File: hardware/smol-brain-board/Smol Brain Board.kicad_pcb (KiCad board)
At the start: 2 copper layers, 67 parts, among them J1 USB4085-GF-A, J10 Jumper 2Way Vert Solderable, J12 Jumper 2Way Vert Solderable, J3 CAN_DBG, J4 Jumper 2Way Vert Solderable, J5 Jumper 2Way Vert Solderable, J6 Smol_Brain_Board, J7 PROGRAM, J8 Jumper 2Way Vert Solderable, J9 Jumper 2Way Vert Solderable, U1 ESP32-S3-WROOM-1-N8, U3 SN65HVD231D

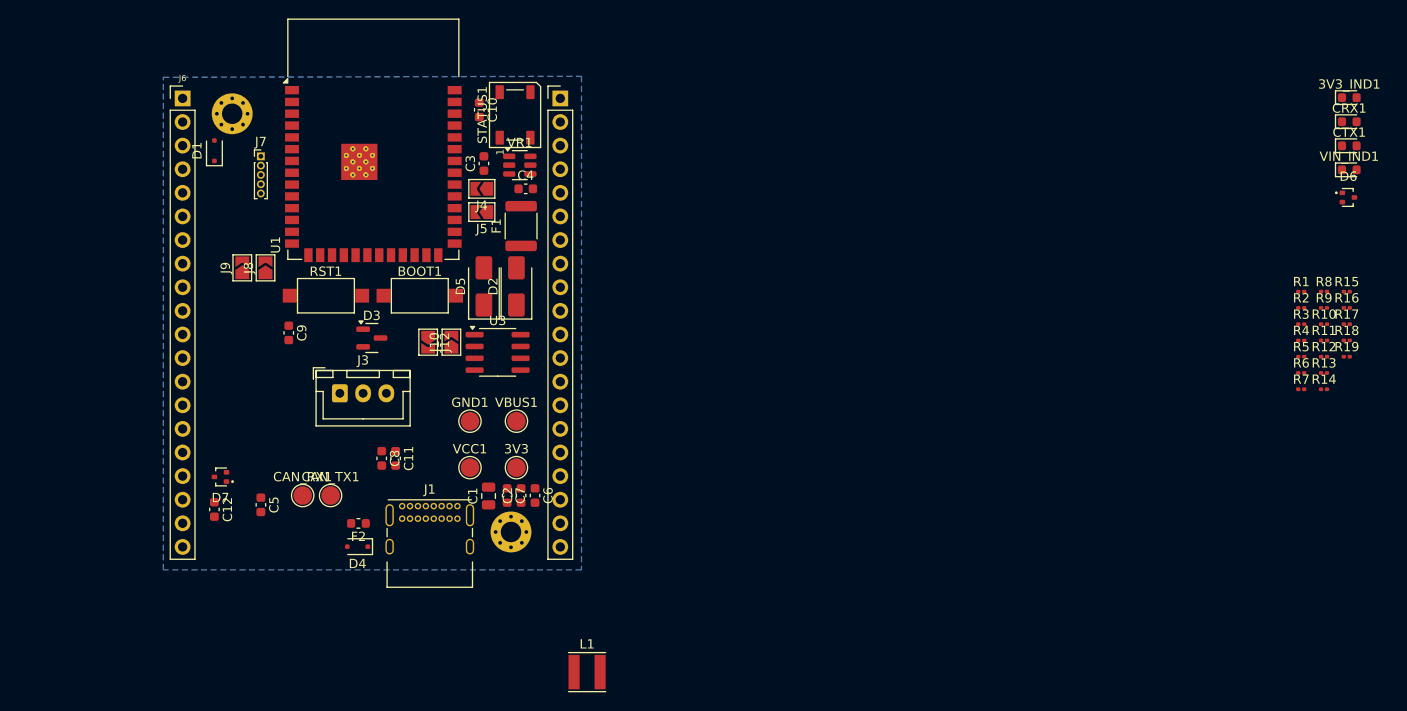
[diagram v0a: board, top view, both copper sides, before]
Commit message: Silkscreen labels and moving stuff around
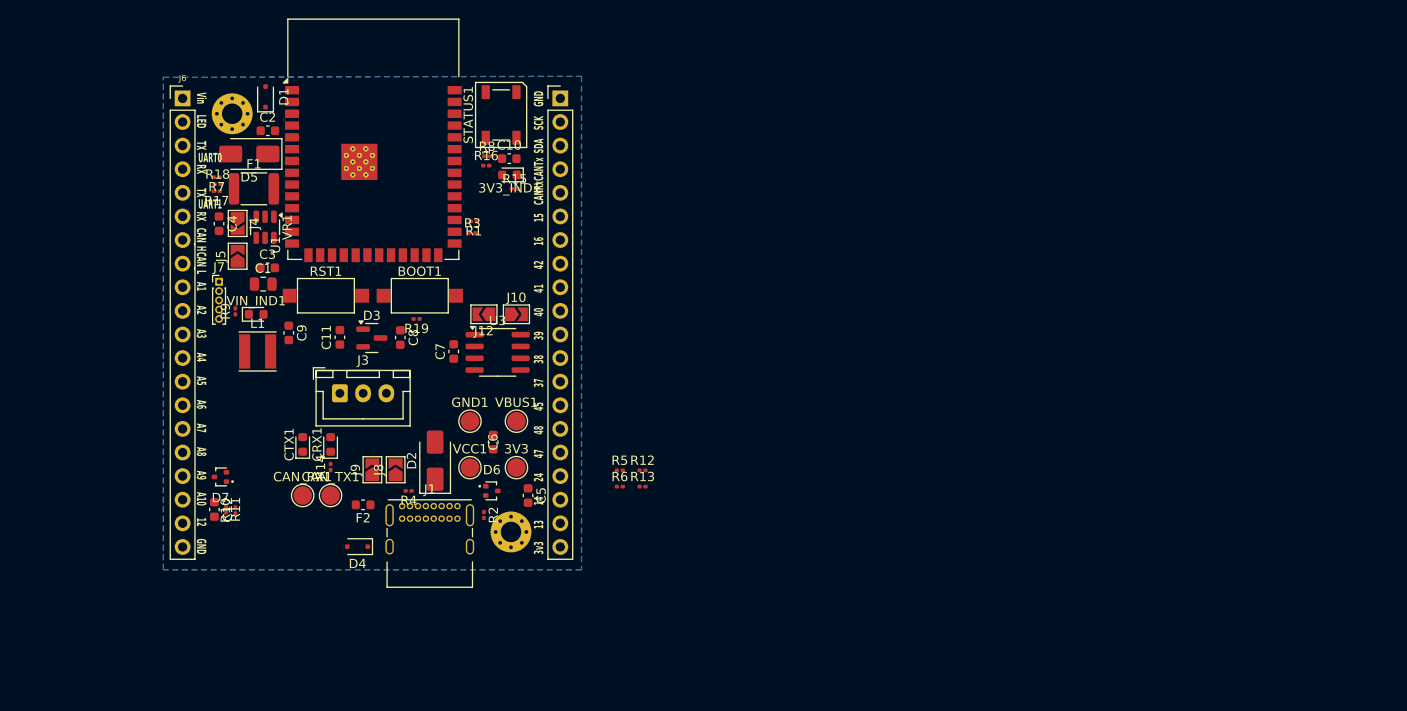
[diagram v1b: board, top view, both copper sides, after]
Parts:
- moved R18 122.7 mm to (131.9, 90.2)
- moved R17 122.4 mm to (131.9, 91.0), turned to 180 degrees
- moved R11 119.5 mm to (132.9, 125.2), turned to -90 degrees
- moved R7 118.9 mm to (131.9, 89.5), turned to 180 degrees
- moved R10 118.8 mm to (133.9, 125.3), turned to 90 degrees
- moved VIN_IND1 118.6 mm to (136.1, 104.2)
- moved R9 117.1 mm to (133.9, 103.9), turned to 90 degrees
- moved CTX1 117.1 mm to (141.1, 118.2), turned to 90 degrees
- moved CRX1 115.0 mm to (144.1, 118.2), turned to 90 degrees
- moved R14 107.2 mm to (144.1, 120.7), turned to 90 degrees
- moved R19 100.2 mm to (153.4, 104.7), turned to 180 degrees
- moved D6 97.4 mm to (161.5, 123.2)
- moved R4 97.4 mm to (152.5, 123.2), turned to 180 degrees
- moved R16 93.9 mm to (160.9, 88.2)
- moved R8 91.2 mm to (160.9, 87.2)
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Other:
- board text added: "12"
- board text added: "13"
- board text added: "14"
- board text added: "15"
- board text added: "16"
- board text added: "24"
- board text added: "37"
- board text added: "38"
- board text added: "39"
- board text added: "3v3"
- board text added: "40"
- board text added: "41"
- board text added: "42"
- board text added: "45"
- board text added: "47"
- board text added: "48"
- board text added: "A1"
- board text added: "A10"
- board text added: "A2"
- board text added: "A3"
- board text added: "A4"
- board text added: "A5"
- board text added: "A6"
- board text added: "A7"
- board text added: "A8"
- board text added: "A9"
- board text added: "CANRx"
- board text added: "CANTx"
- board text added: "CAN_H"
- board text added: "CAN_L"
- board text added: "GND"
- board text added: "LED"
- board text added: "RX"
- board text added: "SCK"
- board text added: "SDA"
- board text added: "TX"
- board text added: "UART0"
- board text added: "UART1"
- board text added: "Vin"

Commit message: Start of routing
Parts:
- removed J10, J4: Jumper 2Way Vert Solderable, Jumper:SolderJumper-2_P1.3mm_Open_TrianglePad1.0x1.5mm
- added JP1: SolderJumper_2_Bridged, Jumper:SolderJumper-2_P1.3mm_Bridged_RoundedPad1.0x1.5mm, F.Cu at (163.4, 103.8)
- added JP2: SolderJumper_2_Bridged, Jumper:SolderJumper-2_P1.3mm_Bridged_RoundedPad1.0x1.5mm, F.Cu at (135.6, 116.7)
- J12, J8, J9: footprint Jumper:SolderJumper-2_P1.3mm_Open_TrianglePad1.0x1.5mm -> Jumper:SolderJumper-2_P1.3mm_Open_RoundedPad1.0x1.5mm
- J5: footprint Jumper:SolderJumper-2_P1.3mm_Open_TrianglePad1.0x1.5mm -> Jumper:SolderJumper-2_P1.3mm_Bridged_RoundedPad1.0x1.5mm
- moved J12 0.43 mm to (160.8, 103.8), turned to 90 degrees
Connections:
- J6 pad 10: A2 -> /A2
- J6 pad 11: A3 -> /A3
- J6 pad 12: A4 -> /A4
- J6 pad 13: A5 -> /A5
- J6 pad 14: A6 -> /A6
- J6 pad 15: A7 -> /A7
- J6 pad 16: A8 -> /A8
- J6 pad 17: A9 -> /A9
- J6 pad 18: A10 -> /A10
- J6 pad 19: IO12 -> /IO12
- J6 pad 2: LED_DOUT -> /LED_DOUT
- J6 pad 22: IO13 -> /IO13
- J6 pad 23: IO14 -> /IO14
- J6 pad 24: IO21 -> /IO21
- J6 pad 25: IO47 -> /IO47
- J6 pad 26: IO48 -> /IO48
- J6 pad 27: IO45 -> /IO45
- J6 pad 28: IO37 -> /IO37
- J6 pad 29: IO38 -> /IO38
- J6 pad 3: UART0_TX -> /UART0_TX
- J6 pad 30: IO39 -> /IO39
- J6 pad 31: IO40 -> /IO40
- J6 pad 32: IO41 -> /IO41
- J6 pad 33: IO42 -> /IO42
- J6 pad 34: IO16 -> /IO16
- J6 pad 35: IO15 -> /IO15
- J6 pad 36: CAN_RX -> /CAN_RX
- J6 pad 37: CAN_TX -> /CAN_TX
- J6 pad 38: I2C_SDA -> /I2C_SDA
- J6 pad 39: I2C_SCK -> /I2C_SCK
- J6 pad 4: UART0_RX -> /UART0_RX
- J6 pad 5: UART1_TX -> /UART1_TX
- J6 pad 6: UART1_RX -> /UART1_RX
- J6 pad 7: CAN_H -> /CAN_H
- J6 pad 8: CAN_L -> /CAN_L
- J6 pad 9: A1 -> /A1
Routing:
- net Net-(J12-A): track 0.00 -> 5.00 mm
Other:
- board outline added: 44.8 x 52.6 mm
- board text added: "-"

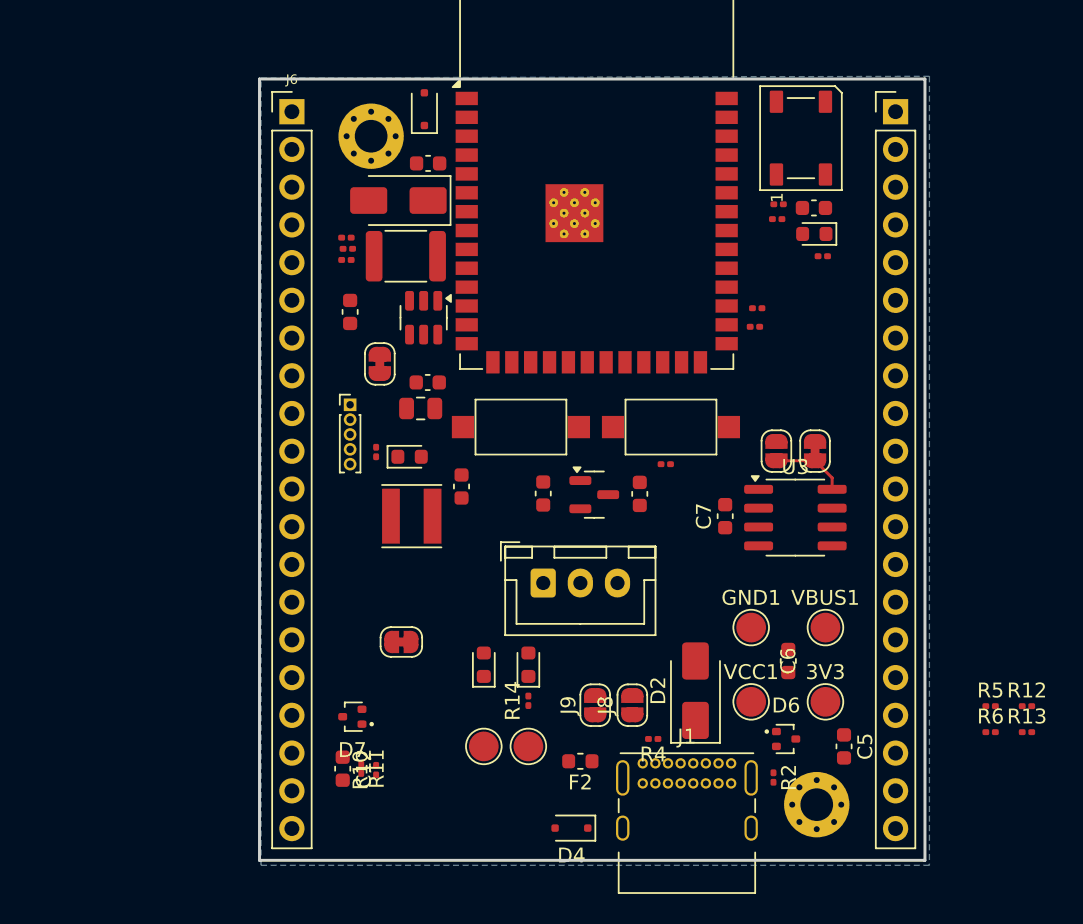
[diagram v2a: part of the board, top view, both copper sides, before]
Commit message: Schematic fixes, foot print and crossovers, continued routing
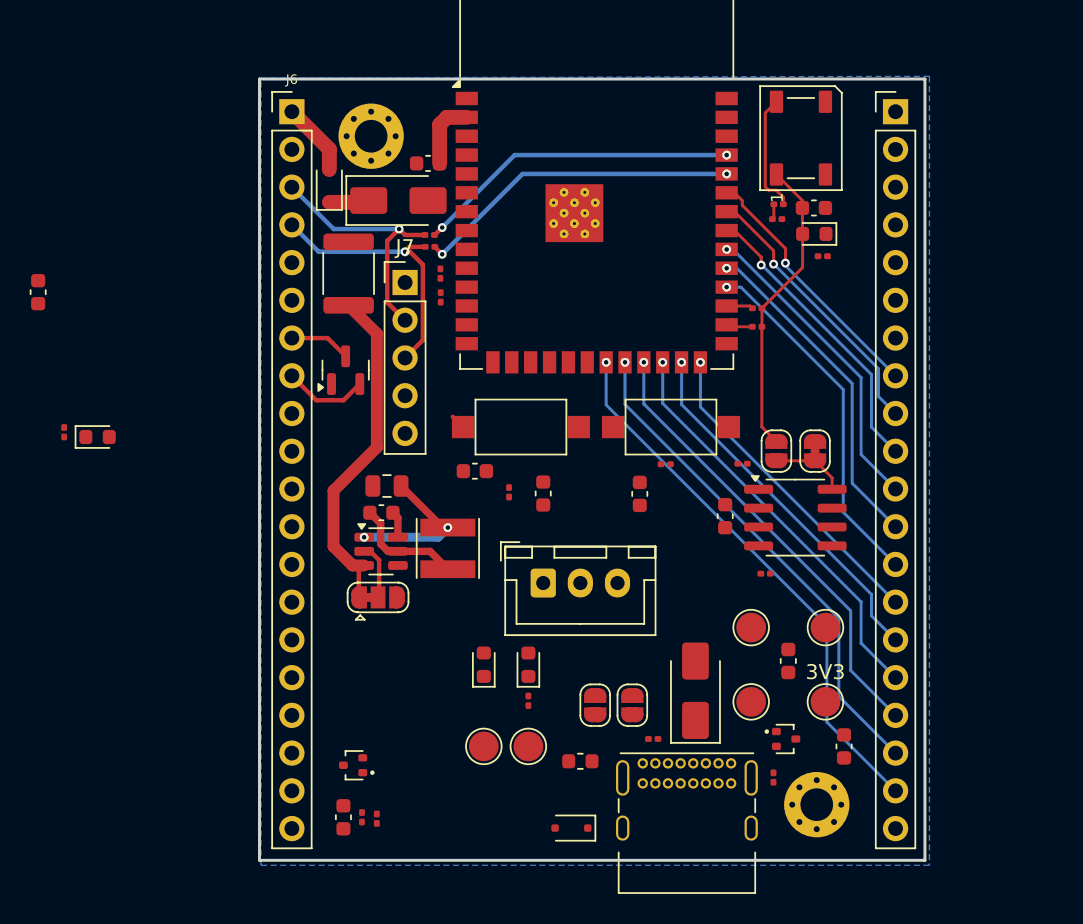
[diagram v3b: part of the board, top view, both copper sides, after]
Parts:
- removed J5: Jumper 2Way Vert Solderable, Jumper:SolderJumper-2_P1.3mm_Bridged_RoundedPad1.0x1.5mm
- removed JP2: SolderJumper_2_Bridged, Jumper:SolderJumper-2_P1.3mm_Bridged_RoundedPad1.0x1.5mm
- added JP3: SolderJumper_3_Bridged12, Jumper:SolderJumper-3_P1.3mm_Bridged12_RoundedPad1.0x1.5mm, F.Cu at (134.0, 113.7)
- J7: footprint Connector_PinHeader_1.00mm:PinHeader_1x05_P1.00mm_Vertical -> Connector_PinHeader_2.54mm:PinHeader_1x05_P2.54mm_Vertical
- moved R5 48.8 mm to (137.5, 90.1)
- moved R6 36.2 mm to (142.8, 106.6), turned to 90 degrees
- moved R13 26.3 mm to (158.5, 104.7)
- moved C4 21.0 mm to (111.1, 93.2)
- moved R9 21.0 mm to (112.8, 102.6)
- moved VIN_IND1 21.0 mm to (115.1, 102.9)
- moved R12 19.7 mm to (160.1, 112.1)
- moved D3 18.7 mm to (131.8, 98.4), turned to 90 degrees
- moved VR1 16.0 mm to (134.2, 110.6), turned to 0 degrees
- moved C3 9.31 mm to (134.2, 108.0)
- moved J7 9.02 mm to (135.8, 92.5)
- moved D1 8.23 mm to (130.7, 86.0)
- moved R17 6.83 mm to (138.2, 93.5), turned to 90 degrees
- moved R18 6.45 mm to (138.2, 91.9), turned to -90 degrees
- moved C1 5.69 mm to (134.6, 106.2)
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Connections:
- R8 pad 2: 3V3 -> Net-(STATUS1-DIN)
- STATUS1 pad 4: 3V3 -> Net-(STATUS1-DIN)
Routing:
- net /IO13: track 0.00 -> 36.9 mm, vias 0 -> 1
- net 3V3: track 0.00 -> 35.4 mm, vias 0 -> 2
- net /IO14: track 0.00 -> 33.9 mm, vias 0 -> 1
- net /IO21: track 0.00 -> 30.8 mm, vias 0 -> 1
- net /IO47: track 0.00 -> 27.7 mm, vias 0 -> 1
- net /IO48: track 0.00 -> 24.7 mm, vias 0 -> 1
- net /IO37: track 0.00 -> 23.9 mm, vias 0 -> 1
- net Net-(JP3-A): track 0.00 -> 23.1 mm
- net /IO38: track 0.00 -> 22.5 mm, vias 0 -> 1
- net Net-(U1-RXD0): track 0.00 -> 22.1 mm, vias 0 -> 2
- net Net-(U1-TXD0): track 0.00 -> 21.9 mm, vias 0 -> 2
- net /IO45: track 0.00 -> 21.6 mm, vias 0 -> 1
- net /IO39: track 0.00 -> 21.1 mm, vias 0 -> 1
- net /IO40: track 0.00 -> 19.9 mm, vias 0 -> 1
- net /IO41: track 0.00 -> 18.6 mm, vias 0 -> 1
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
